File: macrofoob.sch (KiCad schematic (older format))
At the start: 88 parts, among them J1 SSD1306 128x32 OLED, Q1 2N 2222A, SW1 Switch, SW10 Switch, SW11 Switch, SW12 Switch, SW13 Switch, SW14 Switch, SW15 Switch, SW16 Switch, SW17 Switch, SW18 Switch, SW19 Switch, SW2 Switch, SW20 Switch, SW21 Switch, SW22 Switch, SW23 Switch, SW24 Switch, SW25 Switch, SW26 SW_Reset, SW3 Switch, SW4 Switch, SW5 Switch, SW6 Switch, SW7 Switch, SW8 Switch, SW9 Switch, U1 ProMicro

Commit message: first pcb layout and new footprints
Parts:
- RC1, RC2, RC3, RC4: footprint Rotary_Encoder:RotaryEncoder_Alps_EC11E-Switch_Vertical_H20mm -> testatur:RotaryEncoder_Alps_EC11E-Switch_Vertical_H20mm_custom
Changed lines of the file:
@@
 F 0 "RC1" H 7500 1520 50  0000 C CNN
 F 1 "Rotary_Encoder_Switch" H 7500 1427 50  0000 C CNN
-F 2 "Rotary_Encoder:RotaryEncoder_Alps_EC11E-Switch_Vertical_H20mm" H 7350 1310 50  0001 C CNN
+F 2 "testatur:RotaryEncoder_Alps_EC11E-Switch_Vertical_H20mm_custom" H 7350 1310 50  0001 C CNN
 F 3 "~" H 7500 1410 50  0001 C CNN
 	1    7500 1150
@@
 F 0 "RC2" H 10500 1520 50  0000 C CNN
 F 1 "Rotary_Encoder_Switch" H 10500 1427 50  0000 C CNN
-F 2 "Rotary_Encoder:RotaryEncoder_Alps_EC11E-Switch_Vertical_H20mm" H 10350 1310 50  0001 C CNN
+F 2 "testatur:RotaryEncoder_Alps_EC11E-Switch_Vertical_H20mm_custom" H 10350 1310 50  0001 C CNN
 F 3 "~" H 10500 1410 50  0001 C CNN
 	1    10500 1150
@@
 F 0 "RC3" H 7500 6370 50  0000 C CNN
 F 1 "Rotary_Encoder_Switch" H 7500 6277 50  0000 C CNN
-F 2 "Rotary_Encoder:RotaryEncoder_Alps_EC11E-Switch_Vertical_H20mm" H 7350 6160 50  0001 C CNN
+F 2 "testatur:RotaryEncoder_Alps_EC11E-Switch_Vertical_H20mm_custom" H 7350 6160 50  0001 C CNN
 F 3 "~" H 7500 6260 50  0001 C CNN
 	1    7500 6000
@@
 F 0 "RC4" H 10500 6370 50  0000 C CNN
 F 1 "Rotary_Encoder_Switch" H 10500 6277 50  0000 C CNN
-F 2 "Rotary_Encoder:RotaryEncoder_Alps_EC11E-Switch_Vertical_H20mm" H 10350 6160 50  0001 C CNN
+F 2 "testatur:RotaryEncoder_Alps_EC11E-Switch_Vertical_H20mm_custom" H 10350 6160 50  0001 C CNN
 F 3 "~" H 10500 6260 50  0001 C CNN
 	1    10500 6000

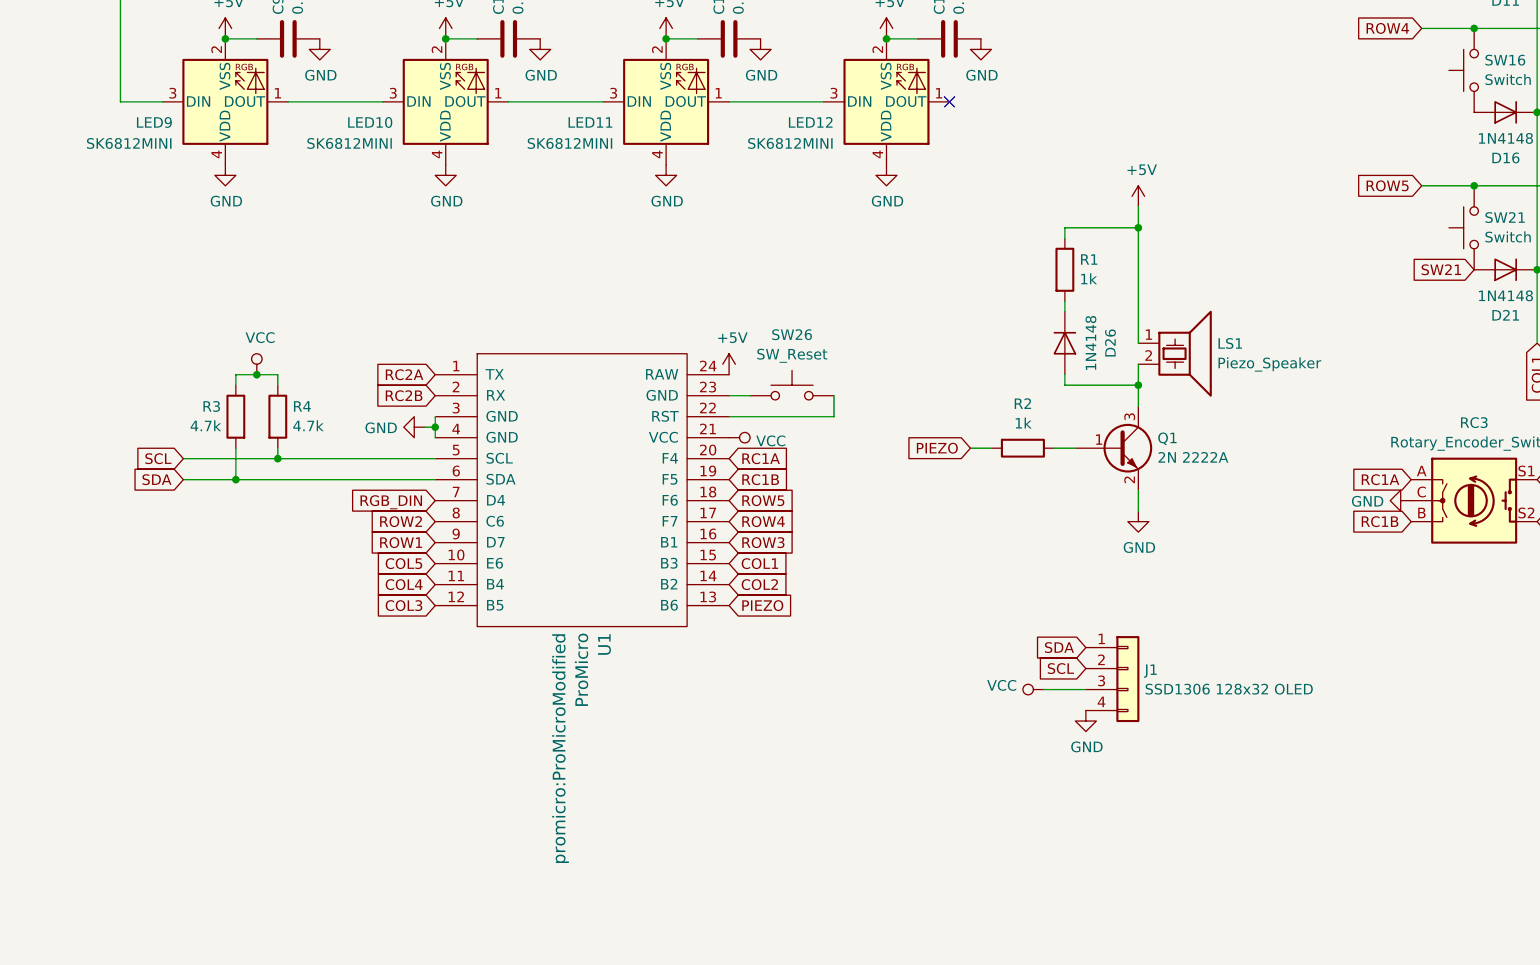
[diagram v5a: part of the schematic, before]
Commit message: replaced the pro micro with a standalone atmega32u4 implementation
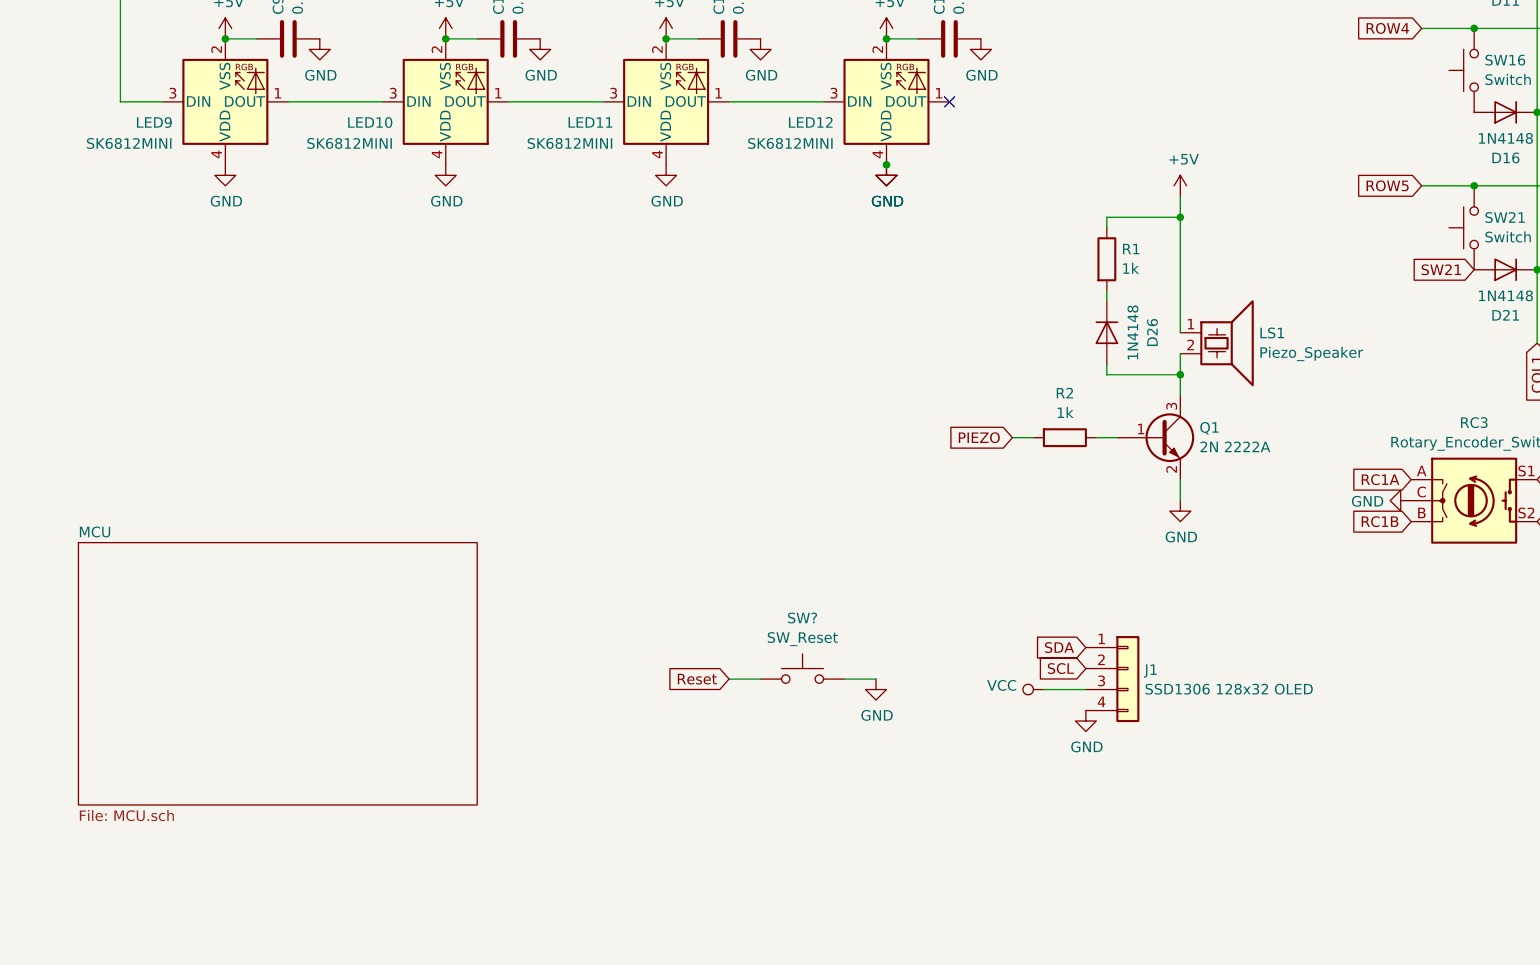
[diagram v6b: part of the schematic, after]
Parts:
- removed R3, R4: 4.7k, Resistor_SMD:R_0805_2012Metric, symbol Device:R
- removed SW26: SW_Reset, Button_Switch_SMD:SW_SPST_PTS810, symbol Switch:SW_Push
- removed U1: ProMicro, promicro:ProMicroModified, symbol promicro:ProMicro
- added SW?: SW_Reset, Button_Switch_SMD:SW_SPST_PTS810, symbol Switch:SW_Push
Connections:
- net GND: now also SW?.2
- new net Reset: SW?.1
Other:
- moved on the sheet: D26, LS1, Q1, R1, R2
